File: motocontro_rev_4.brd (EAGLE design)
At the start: 160 x 89 mm, 36 parts

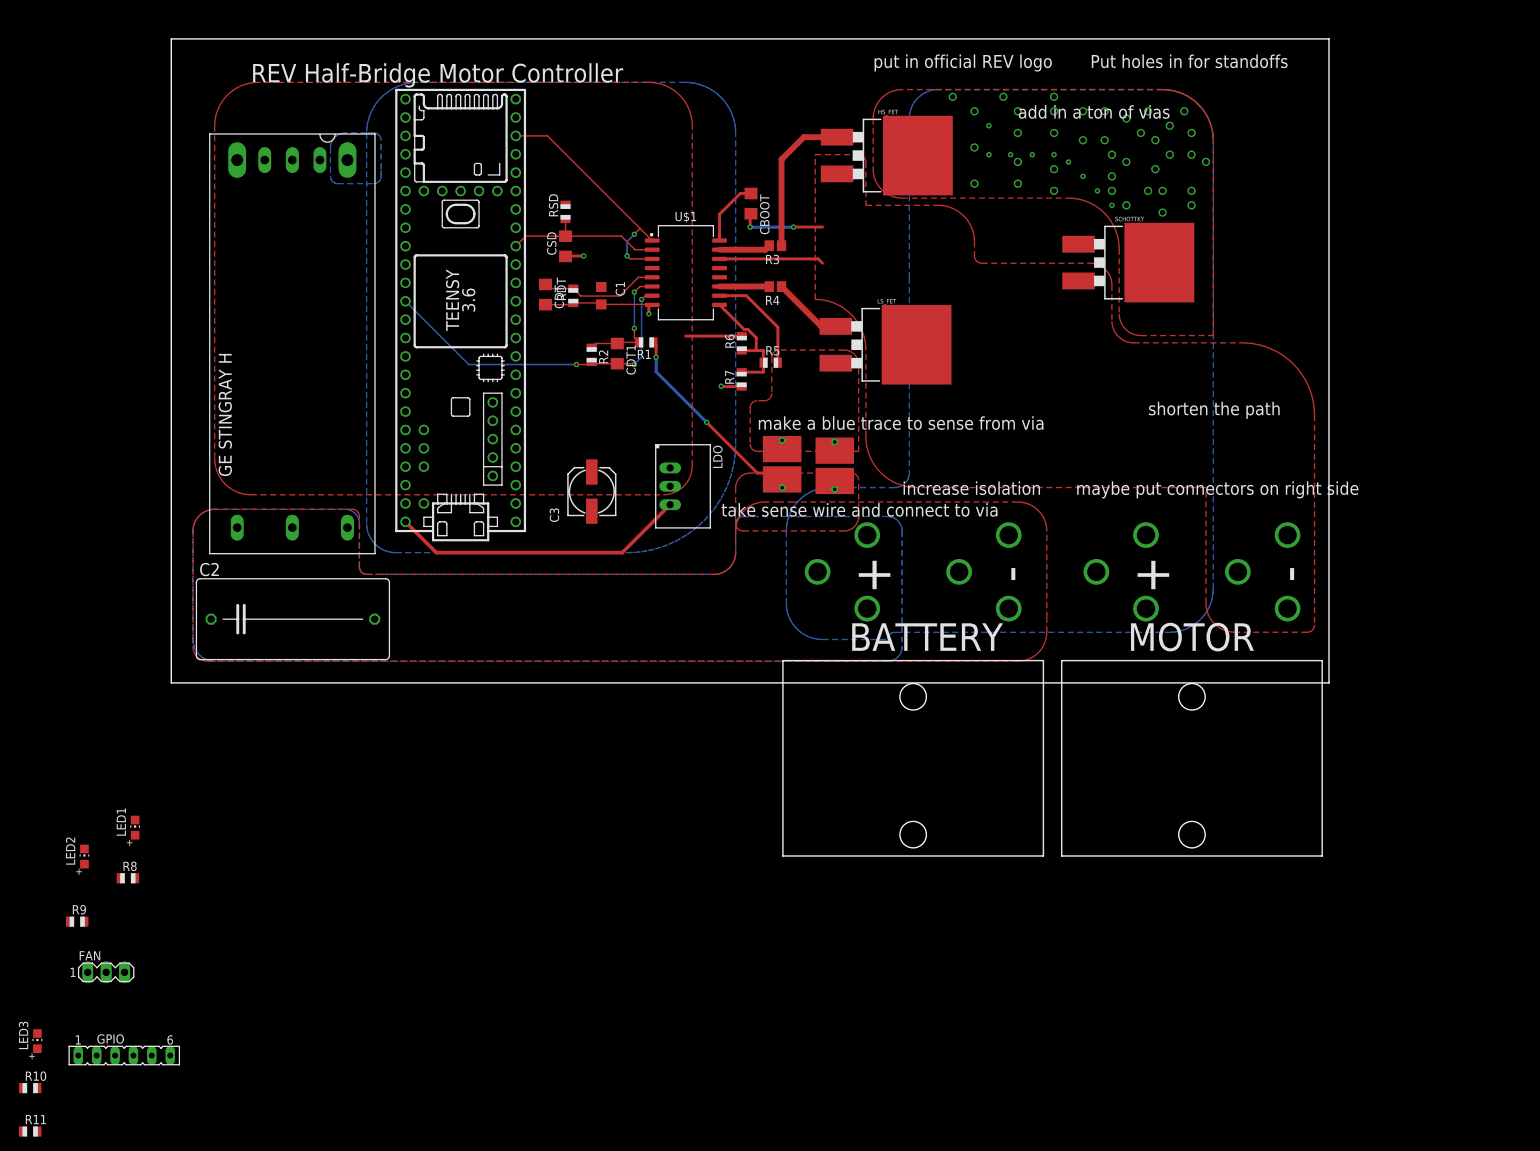
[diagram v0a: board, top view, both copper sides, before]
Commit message: finishes relayout.
Adds test pads, fan connector, GND connections, connects DGND and PGDN. Adds LEDs on power supplies. adds MCU status LED, adds Driver status LED
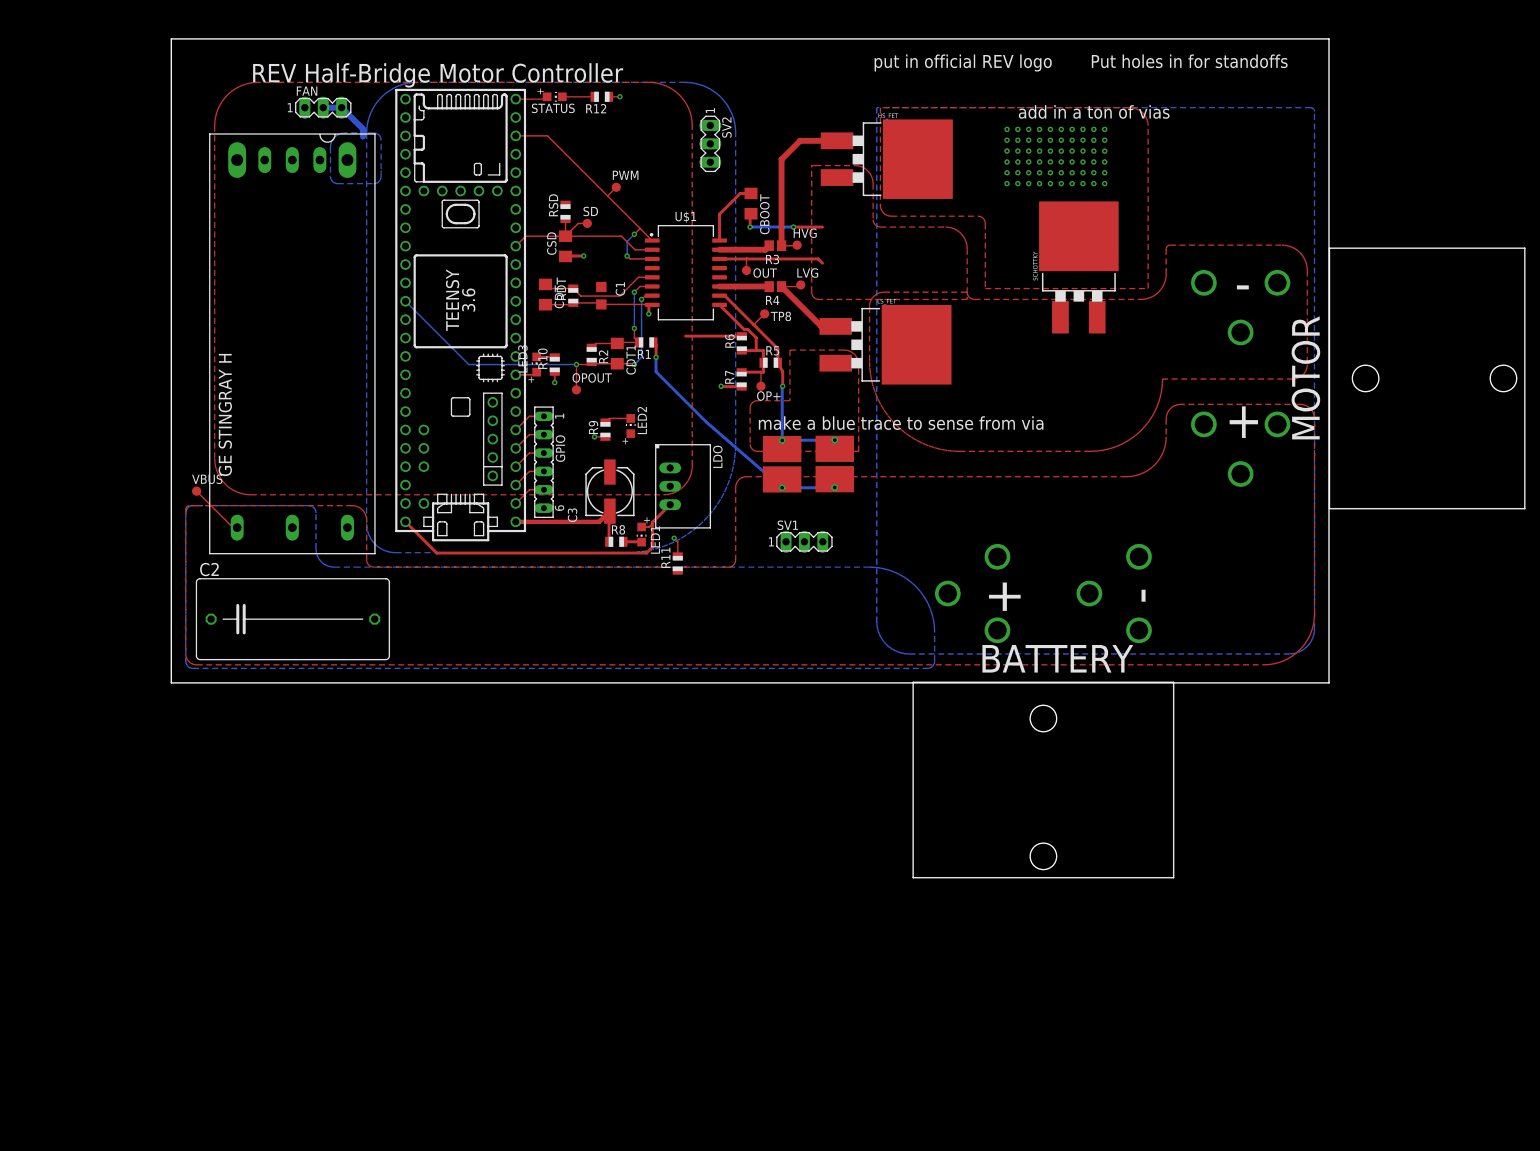
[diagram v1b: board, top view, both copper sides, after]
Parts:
- added HVG, LVG, OP+, OPOUT, OUT, PWM, SD, TP8, VBUS: PTR1B1,27, testpad:B1,27
- added R12: 150, adafruit:R0805
- added STATUS: (no value), adafruit:CHIP-LED0805
- added SV1, SV2: (no value), con-lstb:MA03-1
- moved R10 123.5 mm to (53.0, 44.0), turned to 90 degrees
- moved FAN 123.2 mm to (21.0, 79.5)
- moved R11 119.0 mm to (70.0, 16.5), turned to 90 degrees
- moved LED3 116.2 mm to (50.5, 44.0)
- moved GPIO 100.4 mm to (51.5, 30.5), turned to 270 degrees
- moved R9 99.8 mm to (60.0, 35.0), turned to 90 degrees
- moved LED2 96.1 mm to (63.5, 35.5)
- moved R8 82.0 mm to (61.5, 19.5)
- moved LED1 80.9 mm to (65.0, 20.5), turned to 180 degrees
- moved MOTOR 50.1 mm to (165.1, 42.1), turned to 0 degrees
- moved BATTERY 18.2 mm to (120.5, -4.92)
- moved SCHOTTKY 7.02 mm to (125.4, 57.6), turned to 0 degrees
- moved C3 2.50 mm to (60.6, 26.4)
- moved HS_FET 0.50 mm to (99.1, 72.4)
- moved CURR_RES1 0.25 mm to (94.4, 26.3)
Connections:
- new net N$4: STATUS.A, U$2.32/A13
- new net N$5: R12.2, STATUS.C
- net DGND: now also R12.1, SV2.1, SV2.2, SV2.3
- net N$2: now also HVG.TP
- net N$3: now also LVG.TP
- net OP+: now also OP+.TP
- net OPOUT: now also OPOUT.TP
- net OUT: now also OUT.TP
- net PGND: now also SV1.1, SV1.2, SV1.3
- net PWM: now also PWM.TP
- net RSENSE+: now also TP8.TP
- net SD/OD: now also SD.TP
- net VBUS: now also VBUS.TP
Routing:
- net DGND: track 22.1 -> 55.1 mm, vias 3 -> 7
- net RSENSE+: track 14.8 -> 32.6 mm, vias 0 -> 1
- net PGND: track 26.0 -> 35.2 mm, vias 2 -> 1
- net VBUS: track 1.48 -> 7.70 mm, vias 11 -> 60
- net N$47: track 0.00 -> 4.67 mm
- net N$45: track 0.00 -> 4.67 mm
- net N$44: track 0.00 -> 4.67 mm
- net N$43: track 0.00 -> 4.67 mm
- net N$42: track 0.00 -> 4.67 mm
- net N$4: track 0.00 -> 4.47 mm, vias 1 -> 0
- net N$5: track 0.00 -> 4.45 mm, vias 1 -> 0
- net 5V: track 41.1 -> 44.8 mm
- net SD/OD: track 22.6 -> 26.3 mm
- net N$39: track 0.00 -> 3.73 mm
- net OPOUT: track 46.6 -> 50.1 mm
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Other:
- board text removed: "increase isolation"
- board text removed: "maybe put connectors on right side"
- board text removed: "shorten the path"
- board text removed: "take sense wire and connect to via"

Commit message: Added MOSFET heatsink package
Must re-route and arrange. Probably mess around with making the heatsink smaller or putting an actual heatsink package on top of it.
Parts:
- removed GPIO: (no value), con-lsta:FE06
- added U$4: JST-PH_5-PIN_HEADER, JST_headers:JST_B5B-PH_HEADER
- moved BATTERY 10.0 mm to (120.0, 5.08)
- moved MOTOR 6.50 mm to (158.6, 42.1)
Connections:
- removed net N$47: GPIO.1, U$2.4/CANRX
- net DGND: now also U$4.P5; no longer GPIO.6
- net N$42: now also U$4.P4; no longer GPIO.5
- net N$43: now also U$4.P3; no longer GPIO.4
- net N$44: now also U$4.P2; no longer GPIO.3
- net N$45: now also U$4.P1; no longer GPIO.2
- net OUT: now also LS_FET.P$1, LS_FET.P$10, LS_FET.P$11, LS_FET.P$12, LS_FET.P$13, LS_FET.P$14, LS_FET.P$15, LS_FET.P$16, LS_FET.P$17, LS_FET.P$18, LS_FET.P$19, LS_FET.P$2, LS_FET.P$20, LS_FET.P$21, LS_FET.P$22, LS_FET.P$23, LS_FET.P$24, LS_FET.P$25, LS_FET.P$26, LS_FET.P$27, LS_FET.P$28, LS_FET.P$29, LS_FET.P$3, LS_FET.P$30, LS_FET.P$31, LS_FET.P$32, LS_FET.P$33, LS_FET.P$34, LS_FET.P$35, LS_FET.P$36, LS_FET.P$37, LS_FET.P$38, LS_FET.P$39, LS_FET.P$4, LS_FET.P$40, LS_FET.P$41, LS_FET.P$42, LS_FET.P$43, LS_FET.P$44, LS_FET.P$45, LS_FET.P$46, LS_FET.P$47, LS_FET.P$48, LS_FET.P$49, LS_FET.P$5, LS_FET.P$50, LS_FET.P$51, LS_FET.P$52, LS_FET.P$53, LS_FET.P$54, LS_FET.P$55, LS_FET.P$56, LS_FET.P$57, LS_FET.P$58, LS_FET.P$59, LS_FET.P$6, LS_FET.P$60, LS_FET.P$61, LS_FET.P$62, LS_FET.P$63, LS_FET.P$64, LS_FET.P$65, LS_FET.P$66, LS_FET.P$67, LS_FET.P$68, LS_FET.P$7, LS_FET.P$71, LS_FET.P$72, LS_FET.P$73, LS_FET.P$74, LS_FET.P$78, LS_FET.P$79, LS_FET.P$8, LS_FET.P$80, LS_FET.P$9
- net VBUS: now also HS_FET.P$1, HS_FET.P$10, HS_FET.P$11, HS_FET.P$12, HS_FET.P$13, HS_FET.P$14, HS_FET.P$15, HS_FET.P$16, HS_FET.P$17, HS_FET.P$18, HS_FET.P$19, HS_FET.P$2, HS_FET.P$20, HS_FET.P$21, HS_FET.P$22, HS_FET.P$23, HS_FET.P$24, HS_FET.P$25, HS_FET.P$26, HS_FET.P$27, HS_FET.P$28, HS_FET.P$29, HS_FET.P$3, HS_FET.P$30, HS_FET.P$31, HS_FET.P$32, HS_FET.P$33, HS_FET.P$34, HS_FET.P$35, HS_FET.P$36, HS_FET.P$37, HS_FET.P$38, HS_FET.P$39, HS_FET.P$4, HS_FET.P$40, HS_FET.P$41, HS_FET.P$42, HS_FET.P$43, HS_FET.P$44, HS_FET.P$45, HS_FET.P$46, HS_FET.P$47, HS_FET.P$48, HS_FET.P$49, HS_FET.P$5, HS_FET.P$50, HS_FET.P$51, HS_FET.P$52, HS_FET.P$53, HS_FET.P$54, HS_FET.P$55, HS_FET.P$56, HS_FET.P$57, HS_FET.P$58, HS_FET.P$59, HS_FET.P$6, HS_FET.P$60, HS_FET.P$61, HS_FET.P$62, HS_FET.P$63, HS_FET.P$64, HS_FET.P$65, HS_FET.P$66, HS_FET.P$67, HS_FET.P$68, HS_FET.P$7, HS_FET.P$71, HS_FET.P$72, HS_FET.P$73, HS_FET.P$74, HS_FET.P$78, HS_FET.P$79, HS_FET.P$8, HS_FET.P$80, HS_FET.P$9
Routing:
- net N$47: track 4.67 -> 0.00 mm
- net N$45: track 4.67 -> 2.67 mm
- net N$44: track 4.67 -> 2.67 mm
- net N$43: track 4.67 -> 2.67 mm
- net N$42: track 4.67 -> 2.67 mm
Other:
- board size 160 x 89 mm -> 163 x 89 mm
- board text removed: "add in a ton of vias"
- board text removed: "make a blue trace to sense from via"

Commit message: LETS GO
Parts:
- added C4: 100 u, adafruit:EB20D
- C2: device adafruit:C225-113X268 -> adafruit:EB20D
- moved VBUS 97.2 mm to (100.5, 32.0)
- moved C2 62.5 mm to (79.3, 7.31)
- moved U$4 24.4 mm to (53.0, 29.0), turned to 90 degrees
- moved SCHOTTKY 23.5 mm to (146.4, 68.1)
- moved U$3 3.00 mm to (21.4, 21.5)
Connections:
- net OUT: no longer LS_FET.P$1, LS_FET.P$10, LS_FET.P$11, LS_FET.P$12, LS_FET.P$13, LS_FET.P$14, LS_FET.P$15, LS_FET.P$16, LS_FET.P$17, LS_FET.P$18, LS_FET.P$19, LS_FET.P$2, LS_FET.P$20, LS_FET.P$21, LS_FET.P$22, LS_FET.P$23, LS_FET.P$24, LS_FET.P$25, LS_FET.P$26, LS_FET.P$27, LS_FET.P$28, LS_FET.P$29, LS_FET.P$3, LS_FET.P$30, LS_FET.P$31, LS_FET.P$32, LS_FET.P$33, LS_FET.P$34, LS_FET.P$35, LS_FET.P$36, LS_FET.P$37, LS_FET.P$38, LS_FET.P$39, LS_FET.P$4, LS_FET.P$40, LS_FET.P$41, LS_FET.P$42, LS_FET.P$43, LS_FET.P$44, LS_FET.P$45, LS_FET.P$46, LS_FET.P$47, LS_FET.P$48, LS_FET.P$49, LS_FET.P$5, LS_FET.P$50, LS_FET.P$51, LS_FET.P$52, LS_FET.P$53, LS_FET.P$54, LS_FET.P$55, LS_FET.P$56, LS_FET.P$57, LS_FET.P$58, LS_FET.P$59, LS_FET.P$6, LS_FET.P$60, LS_FET.P$61, LS_FET.P$62, LS_FET.P$63, LS_FET.P$64, LS_FET.P$65, LS_FET.P$66, LS_FET.P$67, LS_FET.P$68, LS_FET.P$7, LS_FET.P$71, LS_FET.P$72, LS_FET.P$73, LS_FET.P$74, LS_FET.P$78, LS_FET.P$79, LS_FET.P$8, LS_FET.P$80, LS_FET.P$9
- net PGND: now also C2.-, C4.-; no longer C2.2
- net VBUS: now also C2.+, C4.+; no longer C2.1, HS_FET.P$1, HS_FET.P$10, HS_FET.P$11, HS_FET.P$12, HS_FET.P$13, HS_FET.P$14, HS_FET.P$15, HS_FET.P$16, HS_FET.P$17, HS_FET.P$18, HS_FET.P$19, HS_FET.P$2, HS_FET.P$20, HS_FET.P$21, HS_FET.P$22, HS_FET.P$23, HS_FET.P$24, HS_FET.P$25, HS_FET.P$26, HS_FET.P$27, HS_FET.P$28, HS_FET.P$29, HS_FET.P$3, HS_FET.P$30, HS_FET.P$31, HS_FET.P$32, HS_FET.P$33, HS_FET.P$34, HS_FET.P$35, HS_FET.P$36, HS_FET.P$37, HS_FET.P$38, HS_FET.P$39, HS_FET.P$4, HS_FET.P$40, HS_FET.P$41, HS_FET.P$42, HS_FET.P$43, HS_FET.P$44, HS_FET.P$45, HS_FET.P$46, HS_FET.P$47, HS_FET.P$48, HS_FET.P$49, HS_FET.P$5, HS_FET.P$50, HS_FET.P$51, HS_FET.P$52, HS_FET.P$53, HS_FET.P$54, HS_FET.P$55, HS_FET.P$56, HS_FET.P$57, HS_FET.P$58, HS_FET.P$59, HS_FET.P$6, HS_FET.P$60, HS_FET.P$61, HS_FET.P$62, HS_FET.P$63, HS_FET.P$64, HS_FET.P$65, HS_FET.P$66, HS_FET.P$67, HS_FET.P$68, HS_FET.P$7, HS_FET.P$71, HS_FET.P$72, HS_FET.P$73, HS_FET.P$74, HS_FET.P$78, HS_FET.P$79, HS_FET.P$8, HS_FET.P$80, HS_FET.P$9
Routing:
- net VBUS: track 7.70 -> 17.0 mm, vias 60 -> 120
- net N$42: track 2.67 -> 6.25 mm
- net N$43: track 2.67 -> 6.03 mm
- net N$44: track 2.67 -> 5.81 mm
- net N$45: track 2.67 -> 5.58 mm
- net OUT: vias 2 -> 98
- added copper zone on layer 16, net OUT
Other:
- board text added: "2mm"
- board text added: "Built with love by M&M"
- board text added: "REV MC 2018.1"
- board text removed: "Put holes in for standoffs"
- board text removed: "REV Half-Bridge Motor Controller"
- board text removed: "put in official REV logo"
